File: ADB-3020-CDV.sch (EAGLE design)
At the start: 117 parts, among them IC1 7812T, IC2 NE555, IC3 LM2576, IC4 NE5532N, IC5 IR2184D, J1 + IN, J2 - IN, J3 - IN, J4 - OUT, J5 PIN2F061.040, J6 + OUT, J7 PIN2F061.040, J8 + IN, Q1 IRFP240-H, Q2 IRFP240-H, T1 BDX53, T2 BC337, T3 BC337, X1-1 LSP13, X1-2 LSP13, X2-1 LSP13, X2-2 LSP13

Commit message: added ne5532 supply pins
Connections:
- net N$28 renamed V-
- new net N$7: IC4P.V-
- net V+: now also IC4P.V+
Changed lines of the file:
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@@
 <setting verticaltext="up"/>
 </settings>
-<grid distance="0.1" unitdist="inch" unit="inch" style="lines" multiple="1" display="no" altdistance="0.01" altunitdist="inch" altunit="inch"/>
+<grid distance="0.01" unitdist="inch" unit="inch" style="lines" multiple="1" display="no" altdistance="0.01" altunitdist="inch" altunit="inch"/>
 <layers>
 <layer number="1" name="Top" color="4" fill="1" visible="no" active="no"/>
@@
 <part name="PAD4" library="solpad" deviceset="LSP13" device=""/>
 <part name="PAD3" library="solpad" deviceset="LSP13" device=""/>
+<part name="P+11" library="supply1" deviceset="V+" device=""/>
+<part name="P-1" library="supply1" deviceset="V-" device=""/>
+<part name="P-2" library="supply1" deviceset="V-" device=""/>
 </parts>
 <sheets>
@@
 <instance part="GND29" gate="1" x="88.646" y="83.82"/>
 <instance part="IC2" gate="G$1" x="39.37" y="83.566"/>
-<instance part="IC4" gate="A" x="67.818" y="42.164"/>
+<instance part="IC4" gate="A" x="67.818" y="42.164" smashed="yes">
+<attribute name="NAME" x="70.358" y="45.339" size="1.778" layer="95"/>
+<attribute name="VALUE" x="72.898" y="39.624" size="1.778" layer="96"/>
+</instance>
 <instance part="IC4" gate="B" x="106.934" y="44.704"/>
 <instance part="Q1" gate="G$1" x="100.584" y="153.162" smashed="yes">
@@
 <attribute name="NAME" x="34.036" y="34.671" size="1.778" layer="95" rot="R180"/>
 </instance>
-<instance part="P+1" gate="1" x="74.93" y="32.258"/>
-<instance part="P+2" gate="1" x="100.33" y="32.004"/>
+<instance part="P+1" gate="1" x="72.39" y="32.258"/>
+<instance part="P+2" gate="1" x="102.87" y="32.004" smashed="yes">
+<attribute name="VALUE" x="105.41" y="32.004" size="1.778" layer="96" rot="R90"/>
+</instance>
 <instance part="P+3" gate="1" x="101.346" y="59.944"/>
 <instance part="P+4" gate="1" x="83.566" y="99.822"/>
@@
 <attribute name="NAME" x="119.38" y="139.319" size="1.778" layer="95"/>
 </instance>
+<instance part="IC4" gate="P" x="86.36" y="35.56" rot="R90"/>
+<instance part="P+11" gate="1" x="78.74" y="30.734" rot="R180"/>
+<instance part="P-1" gate="1" x="93.98" y="30.734"/>
+<instance part="P-2" gate="1" x="74.93" y="75.946" smashed="yes">
+<attribute name="VALUE" x="75.438" y="73.914" size="1.778" layer="96"/>
+</instance>
 </instances>
 <busses>
@@
 </segment>
 </net>
-<net name="N$28" class="0">
-<segment>
-<pinref part="D2" gate="G$1" pin="A"/>
-<pinref part="C21" gate="G$1" pin="2"/>
-<wire x1="62.738" y1="83.566" x2="65.532" y2="83.566" width="0.1524" layer="91"/>
-<wire x1="65.532" y1="83.566" x2="70.612" y2="83.566" width="0.1524" layer="91"/>
-<wire x1="65.532" y1="83.058" x2="65.532" y2="83.566" width="0.1524" layer="91"/>
-<junction x="65.532" y="83.566"/>
-<wire x1="70.612" y1="83.566" x2="74.93" y2="83.566" width="0.1524" layer="91"/>
-<junction x="70.612" y="83.566"/>
-<wire x1="74.93" y1="83.566" x2="74.93" y2="78.486" width="0.1524" layer="91"/>
-</segment>
-</net>
 <net name="N$30" class="0">
 <segment>
@@
 <segment>
 <wire x1="70.358" y1="26.416" x2="70.612" y2="26.416" width="0.1524" layer="91"/>
-<wire x1="70.612" y1="26.416" x2="74.93" y2="26.416" width="0.1524" layer="91"/>
-<wire x1="74.93" y1="26.416" x2="74.93" y2="29.464" width="0.1524" layer="91"/>
+<wire x1="70.612" y1="26.416" x2="72.39" y2="26.416" width="0.1524" layer="91"/>
+<wire x1="72.39" y1="26.416" x2="72.39" y2="29.464" width="0.1524" layer="91"/>
 <pinref part="R32" gate="G$1" pin="1"/>
-<junction x="70.612" y="26.416"/>
 </segment>
 </net>
@@
 <segment>
 <pinref part="R30" gate="G$1" pin="2"/>
-<wire x1="104.902" y1="23.876" x2="100.33" y2="23.876" width="0.1524" layer="91"/>
-<wire x1="100.33" y1="23.876" x2="100.33" y2="29.464" width="0.1524" layer="91"/>
+<wire x1="104.902" y1="23.876" x2="102.87" y2="23.876" width="0.1524" layer="91"/>
+<wire x1="102.87" y1="23.876" x2="102.87" y2="29.464" width="0.1524" layer="91"/>
 <pinref part="P+2" gate="1" pin="V+"/>
 </segment>
@@
 <pinref part="P+10" gate="1" pin="V+"/>
 </segment>
+<segment>
+<pinref part="IC4" gate="P" pin="V+"/>
+<pinref part="P+11" gate="1" pin="V+"/>
+<wire x1="78.74" y1="35.56" x2="78.74" y2="33.274" width="0.1524" layer="91"/>
+</segment>
 </net>
 <net name="N$26" class="0">
@@
 </segment>
 </net>
+<net name="N$7" class="0">
+<segment>
+<pinref part="IC4" gate="P" pin="V-"/>
+<wire x1="93.98" y1="35.56" x2="93.98" y2="33.02" width="0.1524" layer="91"/>
+</segment>
+</net>
+<net name="V-" class="0">
+<segment>
+<pinref part="D2" gate="G$1" pin="A"/>
+<pinref part="C21" gate="G$1" pin="2"/>
+<wire x1="62.738" y1="83.566" x2="65.532" y2="83.566" width="0.1524" layer="91"/>
+<wire x1="65.532" y1="83.566" x2="70.612" y2="83.566" width="0.1524" layer="91"/>
+<wire x1="65.532" y1="83.058" x2="65.532" y2="83.566" width="0.1524" layer="91"/>
+<junction x="65.532" y="83.566"/>
+<wire x1="70.612" y1="83.566" x2="74.93" y2="83.566" width="0.1524" layer="91"/>
+<junction x="70.612" y="83.566"/>
+<wire x1="74.93" y1="83.566" x2="74.93" y2="78.486" width="0.1524" layer="91"/>
+<pinref part="P-2" gate="1" pin="V-"/>
+</segment>
+</net>

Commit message: info added
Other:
- note added: "42V from bridge"
- note added: "V= 1.2-30 A= 0.1-20"

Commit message: Added components values, reviewed some connections
Waiting for a review before merge
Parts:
- removed U$1, U$2: L, adafruit:L
- added L3: 6.8u, adafruit:L
- added L4: 100u, adafruit:L
- B5, B6: value 470u -> 1000u
- B8: value 470u -> 4.7u
- C10, C11, C15, C16, C18, C22, C8: value (none) -> 10n
- C13, C14, C17, C2, C20, C21, C5, C7: value (none) -> 100n
- D1, D2, D3, D4, D6, D7: value (none) -> 1N4148
- LED2: value (none) -> FAULT
- LED3: value (none) -> ON
- LED4: value (none) -> LIMITER
- R1, R22, R30, R32, R35, R36: value (none) -> 10k
- R10, R17, R31, R7, R8: value (none) -> 22k
- R11, R34: value (none) -> 30k
- R12: value (none) -> 15k
- R13, R14, R15, R18, R2, R26, R28, R5, R6, TM2, TM3: value (none) -> 1k
- R16, R21, R23, R3, R4: value (none) -> 4.7k
- R19: value (none) -> 220
- R20: value (none) -> 6.8
- R24, R25: value (none) -> 10m
- R27: value (none) -> 560
- R29: value (none) -> 1M
- R33: value (none) -> 100
- R9: value (none) -> 2.2k
- TM1: value (none) -> 11k
- TM4: value (none) -> 60k
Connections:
- removed net N$61: C16.1, V_FEEDBACK1.1
- removed net N$75: R28.2
- new net N$9: B6.-
- net GND: now also D1.C
- net N$4: now also D6.A
- net N$5: now also R3.2
- net N$73: now also B6.+, C16.1, L3.1, L4.2, V_FEEDBACK1.1; no longer U$1.2, U$2.1
- net N$77: now also L3.2, R28.2; no longer U$2.2
- net VS: now also L4.1; no longer U$1.1
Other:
- moved on the sheet: B1, B10, B2, B3, B5, B6, B7, B8, B9, C1, C10, C11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

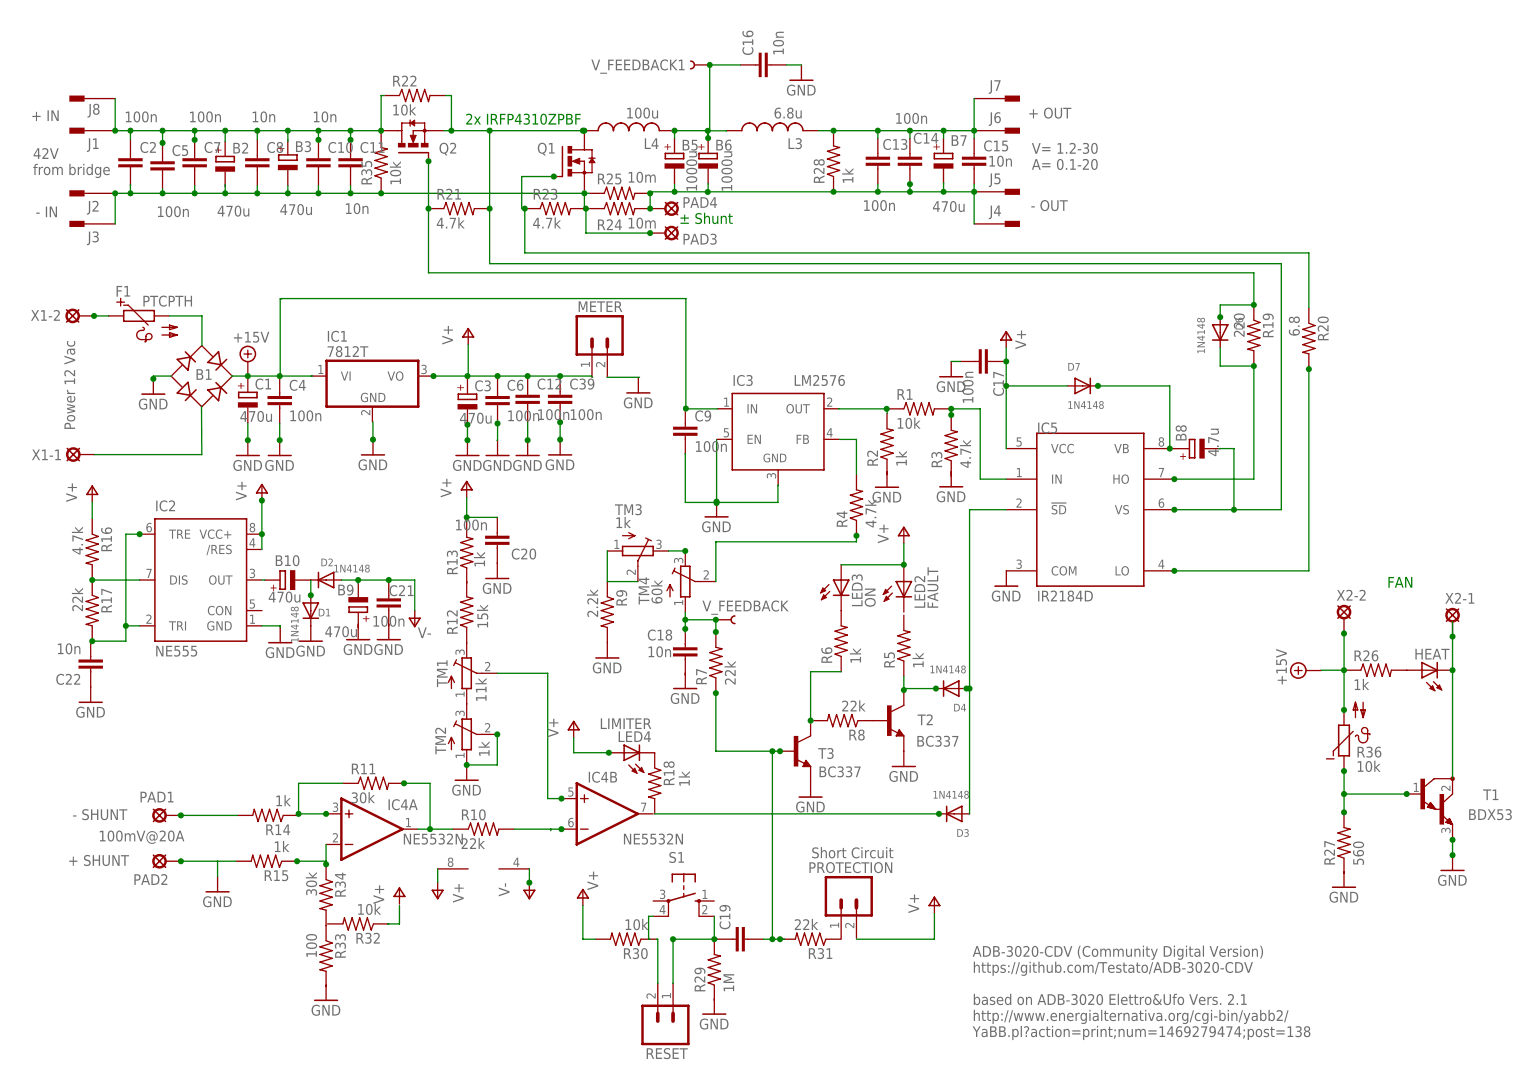
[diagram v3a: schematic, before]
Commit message: Fixed component designators
Fixed components designators to match those in the original schematic and bom
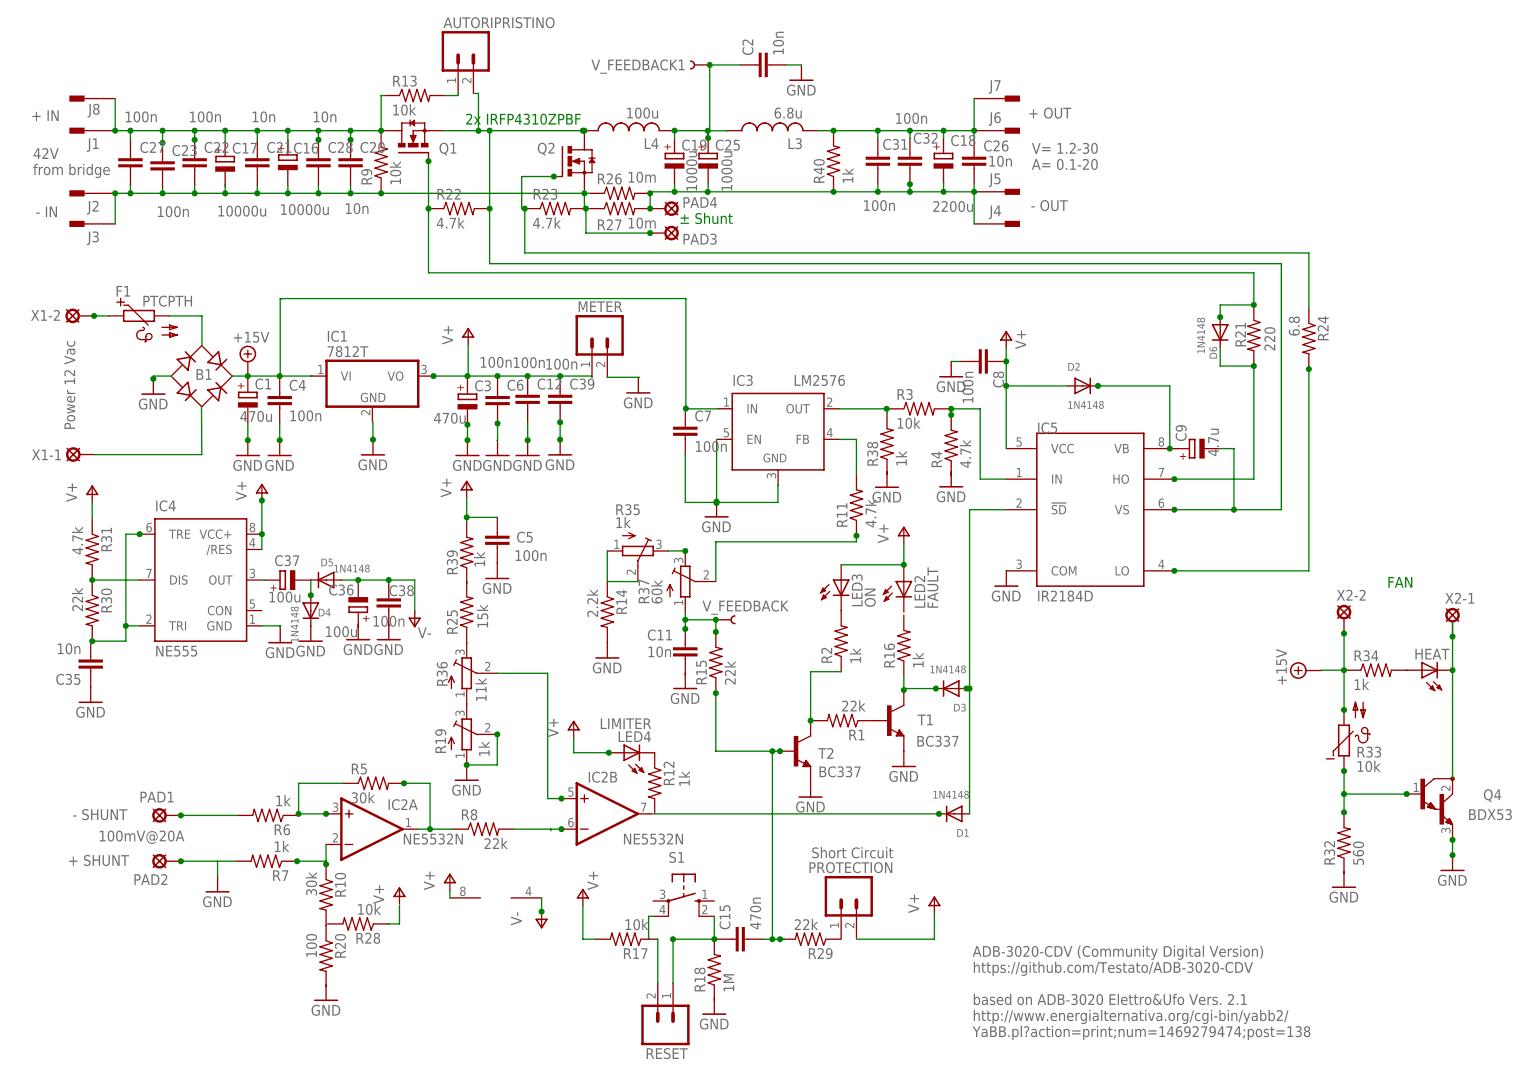
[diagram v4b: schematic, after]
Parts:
- removed B2, B3, B7: 470u, rcl:CPOL-EUE2-5
- removed B5: 1000u, rcl:CPOL-EUE2-5
- removed B8: 4.7u, rcl:CPOL-EUE2-5
- removed D7: 1N4148, adafruit:DIODEDO-1N4148
- removed T3: BC337, transistor:BC337
- removed TM1: 11k, adafruit:TRIMPOT3386
- removed TM2, TM3: 1k, adafruit:TRIMPOT3386
- added AUTORIPRISTINO: (no value), con-amp-quick:MA02
- added C23, C27, C38: 100n, capacitor-wima:C2.5/2
- added C26, C35: 10n, capacitor-wima:C2.5/2
- added D5: 1N4148, adafruit:DIODEDO-1N4148
- added Q4: BDX53, transistor:BDX53
- added R38, R39, R40: 1k, adafruit:R-US_0204/5
- C15: value 10n -> 470n
- C16: value 10n -> 10000u; device capacitor-wima:C2.5/2 -> rcl:CPOL-EUE2-5
- C17: value 100n -> 10000u; device capacitor-wima:C2.5/2 -> rcl:CPOL-EUE2-5
- C18: value 10n -> 2200u; device capacitor-wima:C2.5/2 -> rcl:CPOL-EUE2-5
- C19: value (none) -> 1000u; device capacitor-wima:C2.5/2 -> rcl:CPOL-EUE2-5
- C2, C20, C21: value 100n -> 10n
- C22, C8: value 10n -> 100n
- C36, C37: value 470u -> 100u
- C9: value 100n -> 4.7u; device capacitor-wima:C2.5/2 -> rcl:CPOL-EUE2-5
- IC2: value NE555 -> NE5532N; device st-microelectronics:NE555 -> linear:NE5532N
- IC4: value NE5532N -> NE555; device linear:NE5532N -> st-microelectronics:NE555
- R1, R30: value 10k -> 22k
- R10: value 22k -> 30k
- R11: value 30k -> 4.7k
- R12: value 15k -> 1k
- R13, R28: value 1k -> 10k
- R14: value 1k -> 2.2k
- R15: value 1k -> 22k
- R16: value 4.7k -> 1k
- R17: value 22k -> 10k
- R18: value 1k -> 1M
- R19: value 220 -> 1k; device adafruit:R-US_0204/5 -> adafruit:TRIMPOT3386
- R20: value 6.8 -> 100
- R21: value 4.7k -> 220
- R22: value 10k -> 4.7k
- R24: value 10m -> 6.8
- R25: value 10m -> 15k
- R26: value 1k -> 10m
- R27: value 560 -> 10m
- R29: value 1M -> 22k
- R3: value 4.7k -> 10k
- R31: value 22k -> 4.7k
- R32: value 10k -> 560
- R33: value 100 -> 10k; device adafruit:R-US_0204/5 -> ptc-ntc:NTC640
- R34: value 30k -> 1k
- R35: value 10k -> 1k; device adafruit:R-US_0204/5 -> adafruit:TRIMPOT3386
- R36: value 10k -> 11k; device ptc-ntc:NTC640 -> adafruit:TRIMPOT3386
- R5: value 1k -> 30k
- R7: value 22k -> 1k
- R9: value 2.2k -> 10k
- T1: value BDX53 -> BC337; device transistor:BDX53 -> transistor:BC337
- renumbered B10 to C37, B6 to C25, B9 to C36, C10 to C28, C13 to C31, C14 to C32, TM4 to R37
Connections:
- new net N$8: AUTORIPRISTINO.1, R13.2
- net GND: now also C2.2, C35.1, C5.1, C8.2, D4.C, IC4.GND, Q4.E, R14.2, R19.A, R19.S, R7.2; no longer C16.2, C17.2, C20.1, C22.1, D1.C, IC2.GND, R15.2, R9.2, T3.E, TM2.A, TM2.S
- net N$17: now also C7.2; no longer C9.2
- net N$18: now also IC4.OUT; no longer IC2.OUT
- net N$19: now also R10.2, R20.1; no longer R33.1, R34.2
- net N$20: now also R2.2; no longer R6.2
- net N$21: now also R12.1; no longer R18.1
- net N$22: now also R1.1, T1.B; no longer R8.1, T2.B
- net N$23: now also IC4.DIS, R30.1, R31.2; no longer IC2.DIS, R16.2, R17.1
- net N$24: now also C35.2, IC4.TRE, IC4.TRI, R30.2; no longer C22.2, IC2.TRE, IC2.TRI, R17.2
- net N$25: now also D4.A, D5.C; no longer D1.A, D2.C
- net N$30: now also R25.1, R36.E; no longer R12.1, TM1.E
- net N$31: now also R19.E, R36.A; no longer TM1.A, TM2.E
- net N$32: now also IC2B.+IN, R36.S; no longer IC4B.+IN, TM1.S
- net N$33: now also IC2B.-IN; no longer IC4B.-IN
- net N$34: now also IC2A.OUT, R5.2, R8.1; no longer IC4A.OUT, R10.1, R11.2
- net N$35: now also IC2A.+IN, R5.1, R6.1; no longer IC4A.+IN, R11.1, R14.1
- net N$36: now also IC2A.-IN, R10.1, R7.1; no longer IC4A.-IN, R15.1, R34.1
- net N$37: now also R6.2; no longer R14.2
- net N$38: now also R8.2; no longer R10.2
- net N$39: now also R17.1; no longer R30.1
- net N$4: now also Q1.G, R22.1; no longer Q2.G, R19.1
- net N$40: now also R28.1; no longer R32.1
- net N$42: now also C15.1, R18.2; no longer C19.1, R29.2
- net N$44: now also C15.2, R15.1, R29.2, T2.B; no longer C19.2, R31.2, R7.1, T3.B
- net N$45: now also D1.C, R12.2; no longer D3.C, R18.2
- net N$47: now also R14.1, R35.A, R35.S; no longer R9.1, TM3.A, TM3.S
- net N$48: now also R35.E; no longer TM3.E
- net N$49: now also C11.1, R15.2; no longer C18.1, R7.2
- net N$5: now also R4.2; no longer R1.2
- net N$50: now also R2.1, T2.C; no longer R6.1, T3.C
- net N$51: now also R11.1; no longer R4.1
- net N$52: now also D3.C, R16.1, T1.C; no longer D4.C, R5.1, T2.C
- net N$54: now also D1.A; no longer D4.A
- net N$55: now also R11.2; no longer R4.2
- net N$56: now also R3.1; no longer R1.1
- net N$58: now also C26.2, R26.2, R27.2, R40.1; no longer C15.2, R24.2, R25.2, R28.1
- net N$59: now also D2.C; no longer D7.C
- net N$60: now also R21.2; no longer R19.2
- net N$63: now also C20.1, C21.1, C22.1, C23.1, C27.1, Q1.D, R13.1, R9.2; no longer C11.1, C2.1, C5.1, C7.1, C8.1, Q2.D, R22.1, R35.2
- net N$65: now also R24.2; no longer R20.2
- net N$66: now also Q2.G, R24.1; no longer Q1.G, R20.1
- net N$67: now also R34.2; no longer R26.2
- net N$68: now also Q4.C; no longer T1.C
- net N$69: now also R34.1; no longer R26.1
- net N$7: now also IC2P.V-; no longer IC4P.V-
- net N$71: now also Q4.B, R32.2, R33.1; no longer R27.2, R36.1, T1.B
- net N$72: now also R33.2; no longer R36.2
- net N$73: now also C2.1; no longer C16.1
- net N$74: now also C20.2, C21.2, C22.2, C23.2, C27.2, Q2.S, R26.1, R27.1, R9.1; no longer C11.2, C2.2, C5.2, C7.2, C8.2, Q1.S, R24.1, R25.1, R35.1
- net N$77: now also C26.1, R40.2; no longer C15.1, R28.2
- net V+: now also C5.2, C8.1, D2.A, IC2P.V+, IC4./RES, IC4.VCC+, R17.2, R31.1, R39.2; no longer C17.1, C20.2, D7.A, IC2./RES, IC2.VCC+, IC4P.V+, R13.2, R16.1, R30.2
- net V-: now also C38.2, D5.A; no longer C21.2, D2.A
- net VS: now also AUTORIPRISTINO.2, Q1.S, Q2.D; no longer Q1.D, Q2.S, R21.2
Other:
- moved on the sheet: C11, C15, C2, C20, C21, C22, C5, C7, C8, D1, D2, D3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

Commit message: Fixed some connections
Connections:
- removed net N$25: D4.A, D5.C
- removed net N$43: S1.P1
- removed net N$56: R3.1
- removed net N$59: D2.C
- removed net N$6: IC1.VI
- removed net N$69: R34.1, X2-2.MP
- new net +15V: C4.1, IC1.VI, R34.1, X2-2.MP
- new net N$11: C19.+, C25.+, L4.2
- new net N$12: C37.-, D4.A, D5.C
- new net N$14: R25.2, R39.1
- new net N$15: LED2.C, R16.2
- new net N$16: C7.1, IC3.IN
- new net N$2: B1.AC1, F1.2
- new net VB: C9.+, D2.C, IC5.VB
- net GND: now also C11.2, C12.2, C36.+, C38.1, C6.2, IC1.GND, METER.2, R18.1, R32.1, R38.1, R4.1
- net N$10: now also C37.+, IC4.OUT; no longer C6.2
- net N$13: now also PROTECTION.1, R29.1; no longer IC1.VO
- net N$18: now also IC3.OUT, R3.1, R38.2; no longer IC4.OUT
- net N$19: now also R28.2
- net N$3: now also F1.1
- net N$39: now also RESET.2, S1.P1
- net N$42: now also RESET.1
- net N$45: now also IC2B.OUT
- net N$50: now also R1.2
- net N$58: now also C18.-, C19.-, C25.-
- net N$63: now also C16.+, C17.+
- net N$73: no longer C25.+, L4.2
- net N$74: now also C16.-, C17.-
- net N$77: now also C18.+
- net N$9: now also B1.+, C1.+; no longer C25.-
- net V+: now also C12.1, C3.+, C39.1, C6.1, IC1.VO, METER.1, PROTECTION.2
- net VS: now also C9.-
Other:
- moved on the sheet: C1, C35, C36, C38, C4, C7, LED2, LED3, METER, R17, R20, R28
